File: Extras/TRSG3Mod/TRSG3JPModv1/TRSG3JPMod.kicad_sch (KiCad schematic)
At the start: 3 parts, among them J1 CGA, J2 CONN, U1 2332

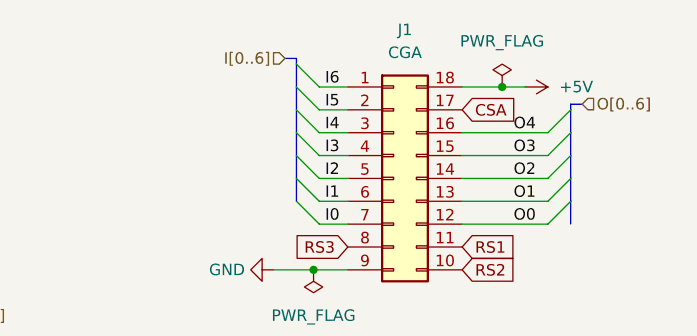
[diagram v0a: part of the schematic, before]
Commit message: Update TRSG3JPMod and Images
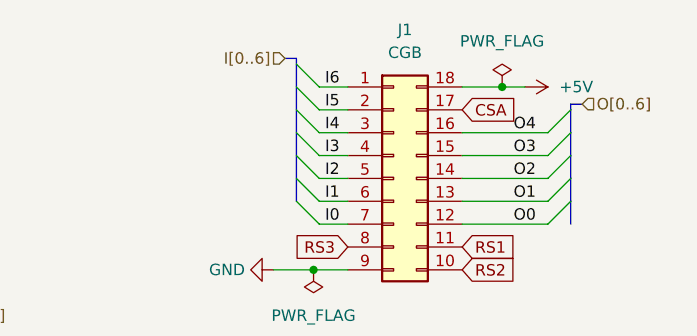
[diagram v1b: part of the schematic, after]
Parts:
- J1: value CGA -> CGB
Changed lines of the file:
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@@
       (effects (font (size 1.27 1.27)))
     )
-    (property "Value" "CGA" (at 158.75 46.99 0)
+    (property "Value" "CGB" (at 158.75 46.99 0)
       (effects (font (size 1.27 1.27)))
     )
